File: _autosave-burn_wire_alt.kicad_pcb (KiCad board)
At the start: 2 copper layers, 24.5 x 24.5 mm, 16 parts, among them J1 TestPoint_THTPad_1.0x1.0mm_Dr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, J2 TestPoint_THTPad_1.0x1.0mm_Dr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, U1 ADP2303ARDZ

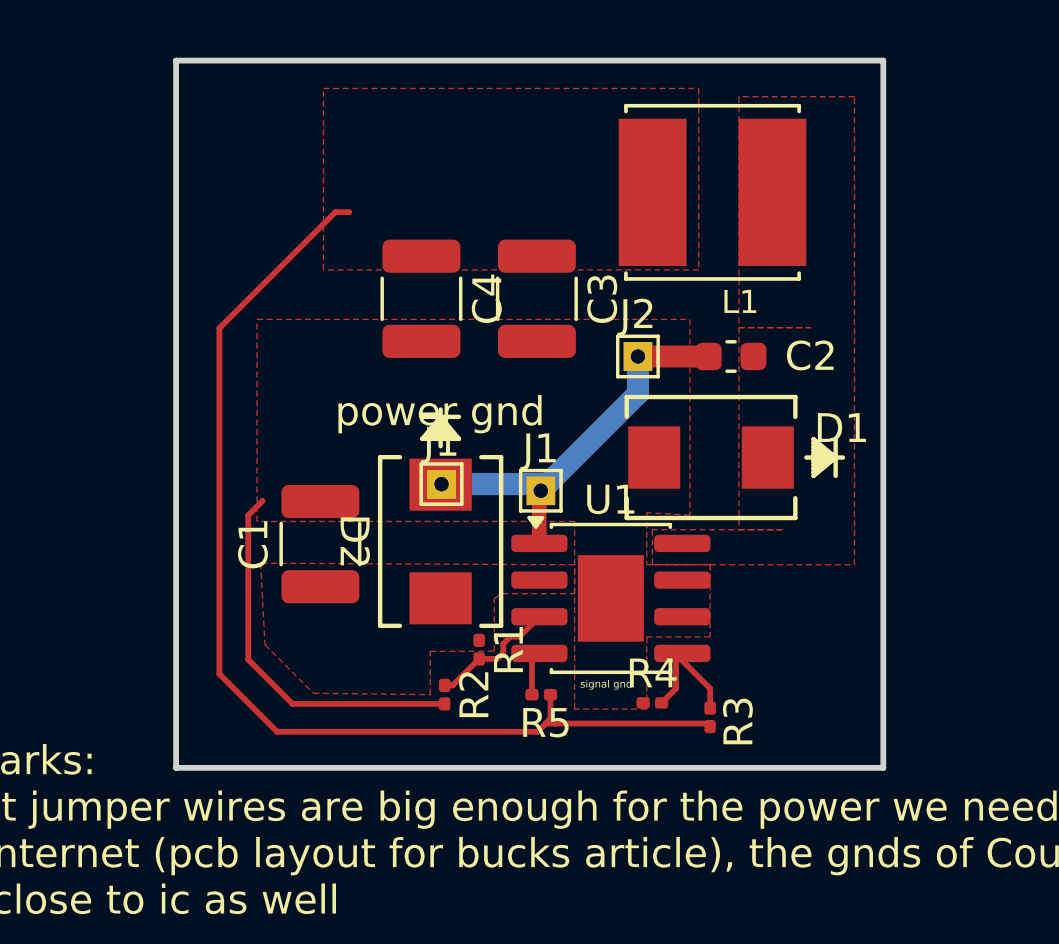
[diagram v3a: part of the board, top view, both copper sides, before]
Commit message: rounded corners
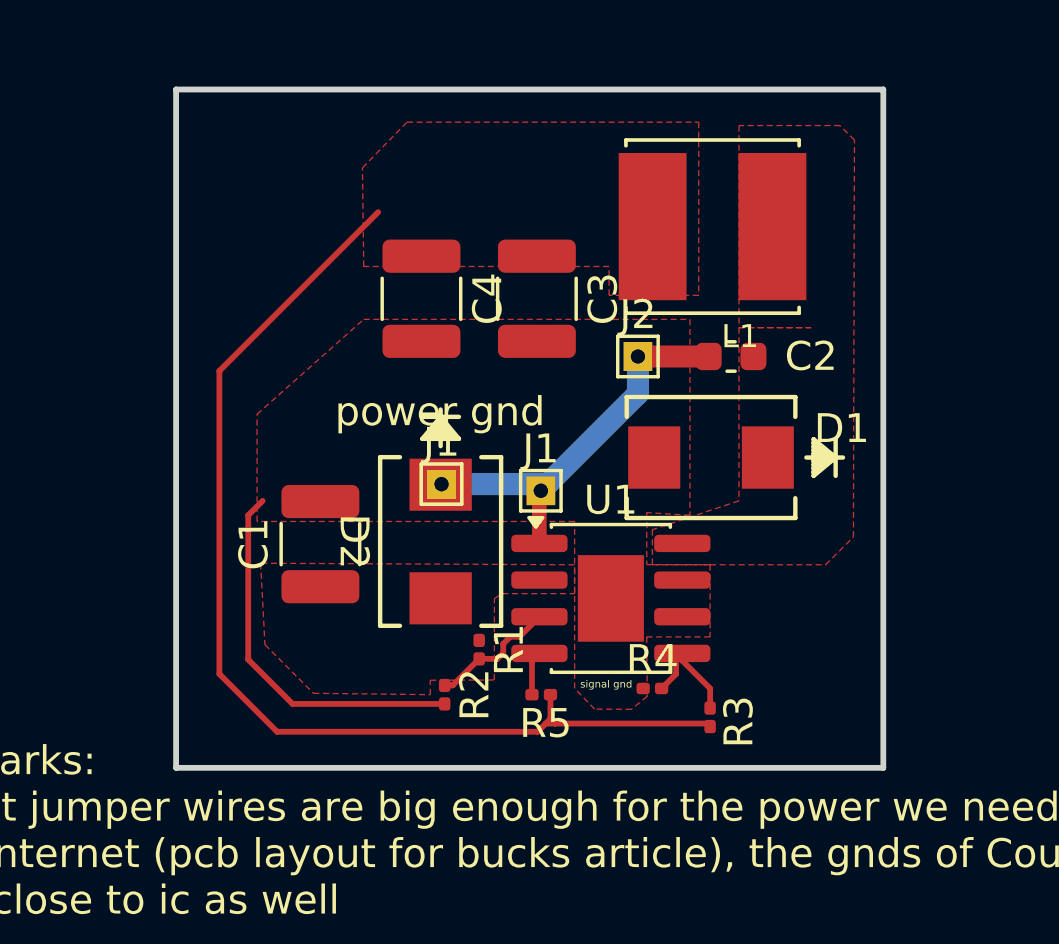
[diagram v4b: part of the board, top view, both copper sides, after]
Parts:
- moved L1 1.19 mm to (174.1, 81.5)
- moved R4 0.50 mm to (172.0, 97.5)
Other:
- board size 24.5 x 24.5 mm -> 24.5 x 23.5 mm
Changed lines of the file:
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@@
 			(layer "F.CrtYd")
 		)
-		(fp_text user "${REFERENCE}"
-			(at 0 -1.45 0)
+		(fp_text user "J3"
+			(at -0.696084 -0.422504 0)
 			(layer "F.Fab")
 			(effects
@@
 	(footprint "imported_footprints:IND_SRN6045TA-3R3Y"
 		(layer "F.Cu")
-		(at 174.083584 80.313715 180)
+		(at 174.083584 81.5 180)
 		(property "Reference" "L1"
 			(at -0.96 -3.808 0)
@@
 	(footprint "Resistor_SMD:R_0201_0603Metric"
 		(layer "F.Cu")
-		(at 172 98 180)
+		(at 172 97.5 180)
 		(descr "Resistor SMD 0201 (0603 Metric), square (rectangular) end terminal, IPC-7351 nominal, (Body size source: https://www.vishay.com/docs/20052/crcw0201e3.pdf)")
 		(tags "resistor")
@@
 	)
 	(gr_rect
-		(start 155.5 75.75)
+		(start 155.5 76.75)
 		(end 179.999999 100.25)
 		(stroke
@@
 	)
 	(segment
-		(start 168.47013 98.54987)
-		(end 168.63513 98.71487)
-		(width 0.2)
-		(layer "F.Cu")
-		(net "/Vout")
-	)
-	(segment
-		(start 161.02 81)
-		(end 157 85.02)
-		(width 0.2)
-		(layer "F.Cu")
-		(net "/Vout")
-	)
-	(segment
-		(start 168.47013 97.71487)
-		(end 168.47013 98.54987)
-		(width 0.2)
-		(layer "F.Cu")
-		(net "/Vout")
-	)
-	(segment
-		(start 168.02 99)
-		(end 168.30513 98.71487)
-		(width 0.2)
-		(layer "F.Cu")
-		(net "/Vout")
-	)
-	(segment
-		(start 159 99)
-		(end 168.02 99)
-		(width 0.2)
-		(layer "F.Cu")
-		(net "/Vout")
-	)
-	(segment
-		(start 173.89487 98.71487)
-		(end 168.63513 98.71487)
-		(width 0.2)
-		(layer "F.Cu")
-		(net "/Vout")
-	)
-	(segment
-		(start 157 85.02)
-		(end 157 97)
-		(width 0.2)
-		(layer "F.Cu")
-		(net "/Vout")
-	)
-	(segment
-		(start 168.30513 98.71487)
-		(end 168.63513 98.71487)
-		(width 0.2)
-		(layer "F.Cu")
-		(net "/Vout")
-	)
-	(segment
-		(start 161.5 81)
-		(end 161.02 81)
-		(width 0.2)
-		(layer "F.Cu")
-		(net "/Vout")
-	)
-	(segment
-		(start 174 98.82)
-		(end 173.89487 98.71487)
-		(width 0.2)
-		(layer "F.Cu")
-		(net "/Vout")
-	)
-	(segment
-		(start 168.47013 98.54987)
-		(end 168.30513 98.71487)
-		(width 0.2)
-		(layer "F.Cu")
-		(net "/Vout")
-	)
-	(segment
-		(start 157 97)
-		(end 159 99)
-		(width 0.2)
-		(layer "F.Cu")
-		(net "/Vout")
-	)
-	(segment
-		(start 158 96.5)
-		(end 158 91.5)
-		(width 0.2)
-		(layer "F.Cu")
-		(net "GND")
-	)
-	(segment
-		(start 158 91.5)
-		(end 158.5 91)
-		(width 0.2)
-		(layer "F.Cu")
-		(net "GND")
-	)
-	(segment
-		(start 164.80513 98.03487)
-		(end 159.53487 98.03487)
-		(width 0.2)
-		(layer "F.Cu")
-		(net "GND")
-	)
-	(segment
-		(start 159.53487 98.03487)
-		(end 158 96.5)
-		(width 0.2)
-		(layer "F.Cu")
-		(net "GND")
-	)
-	(segment
 		(start 168.136714 90.651297)
 		(end 168.081839 90.706172)
@@
 	)
 	(segment
+		(start 162.5 81)
+		(end 157 86.5)
+		(width 0.2)
+		(layer "F.Cu")
+		(net "/Vout")
+	)
+	(segment
+		(start 168.47013 98.54987)
+		(end 168.63513 98.71487)
+		(width 0.2)
+		(layer "F.Cu")
+		(net "/Vout")
+	)
+	(segment
+		(start 157 97)
+		(end 159 99)
+		(width 0.2)
+		(layer "F.Cu")
+		(net "/Vout")
+	)
+	(segment
+		(start 168.47013 97.71487)
+		(end 168.47013 98.54987)
+		(width 0.2)
+		(layer "F.Cu")
+		(net "/Vout")
+	)
+	(segment
+		(start 157 86.5)
+		(end 157 97)
+		(width 0.2)
+		(layer "F.Cu")
+		(net "/Vout")
+	)
+	(segment
+		(start 168.02 99)
+		(end 168.30513 98.71487)
+		(width 0.2)
+		(layer "F.Cu")
+		(net "/Vout")
+	)
+	(segment
+		(start 173.89487 98.71487)
+		(end 168.63513 98.71487)
+		(width 0.2)
+		(layer "F.Cu")
+		(net "/Vout")
+	)
+	(segment
+		(start 168.30513 98.71487)
+		(end 168.63513 98.71487)
+		(width 0.2)
+		(layer "F.Cu")
+		(net "/Vout")
+	)
+	(segment
+		(start 174 98.82)
+		(end 173.89487 98.71487)
+		(width 0.2)
+		(layer "F.Cu")
+		(net "/Vout")
+	)
+	(segment
+		(start 168.47013 98.54987)
+		(end 168.30513 98.71487)
+		(width 0.2)
+		(layer "F.Cu")
+		(net "/Vout")
+	)
+	(segment
+		(start 159 99)
+		(end 168.02 99)
+		(width 0.2)
+		(layer "F.Cu")
+		(net "/Vout")
+	)
+	(segment
+		(start 158 96.5)
+		(end 158 91.5)
+		(width 0.2)
+		(layer "F.Cu")
+		(net "GND")
+	)
+	(segment
+		(start 158 91.5)
+		(end 158.5 91)
+		(width 0.2)
+		(layer "F.Cu")
+		(net "GND")
+	)
+	(segment
+		(start 164.80513 98.03487)
+		(end 159.53487 98.03487)
+		(width 0.2)
+		(layer "F.Cu")
+		(net "GND")
+	)
+	(segment
+		(start 159.53487 98.03487)
+		(end 158 96.5)
+		(width 0.2)
+		(layer "F.Cu")
+		(net "GND")
+	)
+	(segment
 		(start 166.833811 96.26841)
 		(end 166.627221 96.475)
@@
 	)
 	(segment
-		(start 172.82 97.5)
-		(end 172.82 96.502221)
-		(width 0.2)
-		(layer "F.Cu")
-		(net "/FB")
-	)
-	(segment
 		(start 173.036611 96.536611)
 		(end 174 97.5)
@@
 	)
 	(segment
-		(start 172.32 98)
-		(end 172.82 97.5)
+		(start 172.82 96.502221)
+		(end 173.036611 96.28561)
+		(width 0.2)
+		(layer "F.Cu")
+		(net "/FB")
+	)
+	(segment
+		(start 172.32 97.5)
+		(end 172.82 97)
+		(width 0.2)
+		(layer "F.Cu")
+		(net "/FB")
+	)
+	(segment
+		(start 172.82 97)
+		(end 172.82 96.502221)
 		(width 0.2)
 		(layer "F.Cu")
@@
 		(start 174 97.5)
 		(end 174 98.18)
-		(width 0.2)
-		(layer "F.Cu")
-		(net "/FB")
-	)
-	(segment
-		(start 172.82 96.502221)
-		(end 173.036611 96.28561)
 		(width 0.2)
 		(layer "F.Cu")
@@
 		(polygon
 			(pts
-				(xy 158.30513 84.71487) (xy 170.30513 84.71487) (xy 170.305137 84.71487) (xy 173.303604 84.71487)
+				(xy 158.30513 88) (xy 162 84.71487) (xy 170.30513 84.71487) (xy 170.305137 84.71487) (xy 173.303604 84.71487)
 				(xy 173.304518 91.5) (xy 171.80513 91.409245) (xy 171.80513 93.208563) (xy 174 93.212518) (xy 174 95.71487)
-				(xy 171.80513 95.71487) (xy 171.80513 98.21487) (xy 169.30513 98.21487) (xy 169.30513 91.71487)
-				(xy 158.30513 91.71487)
+				(xy 171.80513 95.71487) (xy 171.821184 97.772697) (xy 171.273974 98.222932) (xy 170 98.21487) (xy 169.30513 97.5)
+				(xy 169.30513 91.71487) (xy 158.30513 91.71487)
 			)
 		)
@@
 		(polygon
 			(pts
-				(xy 173.60523 76.71487) (xy 173.60523 83) (xy 160.60523 83) (xy 160.60523 76.71487)
+				(xy 163.5 77.881501) (xy 173.60523 77.881501) (xy 173.60523 83.881501) (xy 170.5 83.881501) (xy 170.5 82.881501)
+				(xy 162 82.881501) (xy 161.956651 79.464511)
 			)
 		)
@@
 			(pts
 				(xy 169.30513 93.21487) (xy 158.429005 93.161993) (xy 158.578707 95.98336) (xy 160.258882 97.667374)
-				(xy 164.30513 97.71487) (xy 164.30513 96.214873) (xy 166.524562 96.207723) (xy 166.524562 94.385344)
+				(xy 164.30513 97.71487) (xy 164.30513 97.214876) (xy 166.524562 97.207726) (xy 166.524562 94.385344)
 				(xy 166.80513 94.21487) (xy 169.30513 94.21487)
 			)
@@
 		(polygon
 			(pts
-				(xy 172 92) (xy 172 93.21487) (xy 179 93.21487) (xy 179 77) (xy 175 77) (xy 175 85) (xy 177.5 85)
-				(xy 175 85) (xy 175 92) (xy 176.5 92)
-			)
-		)
+				(xy 172 92) (xy 172 93.21487) (xy 178 93.21487) (xy 178.964196 92.255505) (xy 179 78.5) (xy 178.5 78)
+				(xy 175 78) (xy 175 85) (xy 177.5 85) (xy 175 85) (xy 175 91)
+			)
+		)

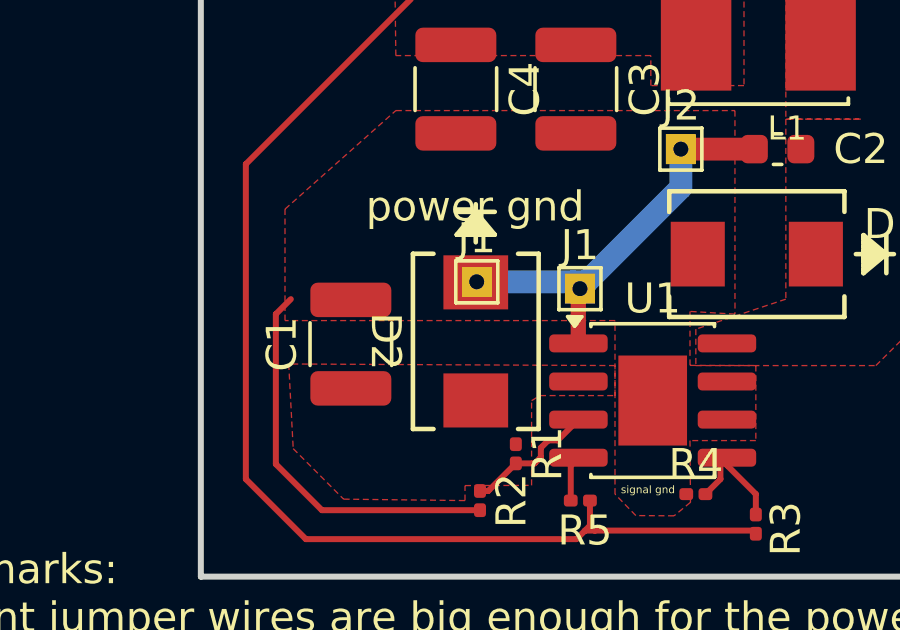
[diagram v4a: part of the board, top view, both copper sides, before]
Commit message: added bst plane under bst diode
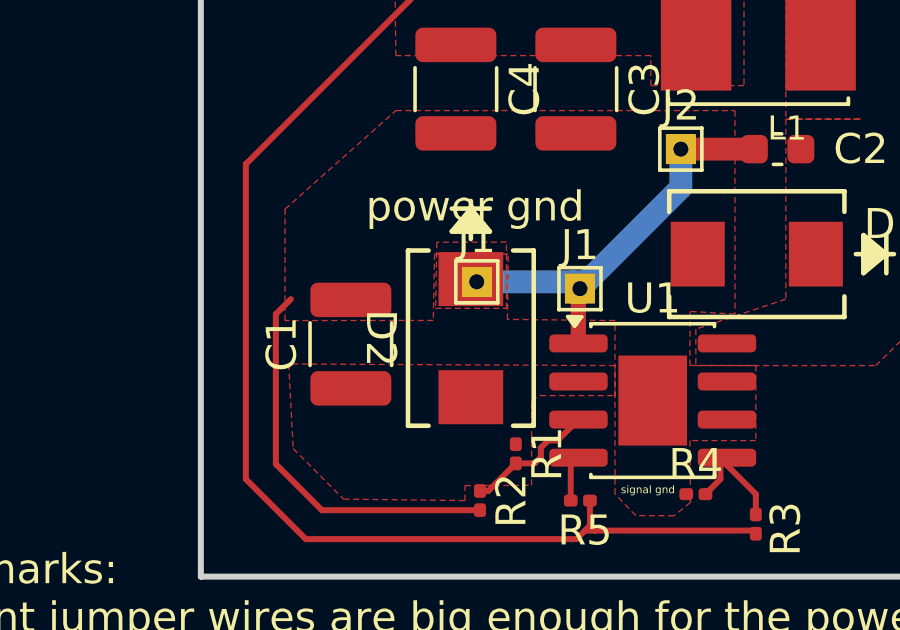
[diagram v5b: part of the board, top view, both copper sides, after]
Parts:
- moved D2 0.20 mm to (164.5, 92.3)
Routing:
- added copper zone on F.Cu, net /BST
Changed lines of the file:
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@@
 	(footprint "imported_footprints:CR_SMB_320-345BE_DIO-L"
 		(layer "F.Cu")
-		(at 164.664534 92.408744 -90)
+		(at 164.5 92.3001 -90)
 		(tags "B330B-13-F ")
 		(property "Reference" "D2"
@@
 				(xy 173.304518 91.5) (xy 171.80513 91.409245) (xy 171.80513 93.208563) (xy 174 93.212518) (xy 174 95.71487)
 				(xy 171.80513 95.71487) (xy 171.821184 97.772697) (xy 171.273974 98.222932) (xy 170 98.21487) (xy 169.30513 97.5)
-				(xy 169.30513 91.71487) (xy 158.30513 91.71487)
-			)
-		)
+				(xy 169.30513 91.71487) (xy 165.72021 91.67415) (xy 165.744922 89.498664) (xy 163.29022 89.500218)
+				(xy 163.249204 91.710216) (xy 158.30513 91.71487)
+			)
+		)
+	)
+	(zone
+		(net "/BST")
+		(layer "F.Cu")
+		(hatch edge 0.5)
+		(connect_pads yes
+			(clearance 0.254)
+		)
+		(min_thickness 0.25)
+		(fill yes
+			(thermal_gap 0.5)
+			(thermal_bridge_width 0.5)
+			(island_removal_mode 0)
+		)
+		(polygon
+			(pts
+				(xy 163.366117 89.103415) (xy 163.325102 91.306783) (xy 165.687756 91.306783) (xy 165.687756 89.098543)
+			)
+		)

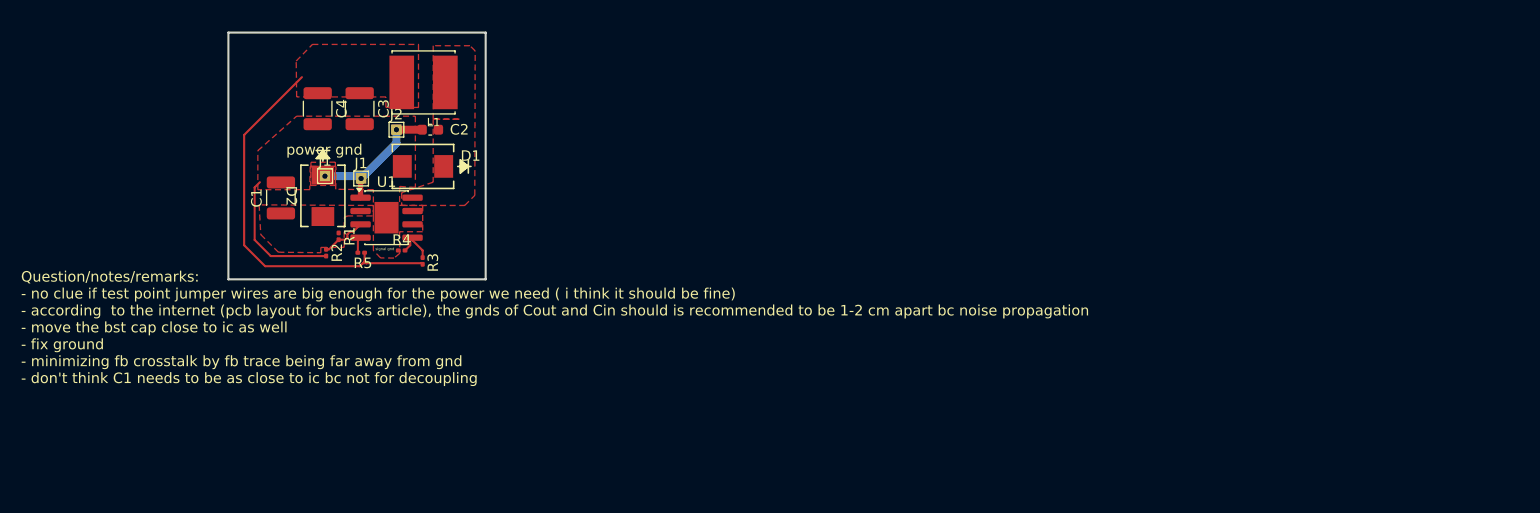
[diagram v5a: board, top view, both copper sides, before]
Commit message: cout connected to agnd
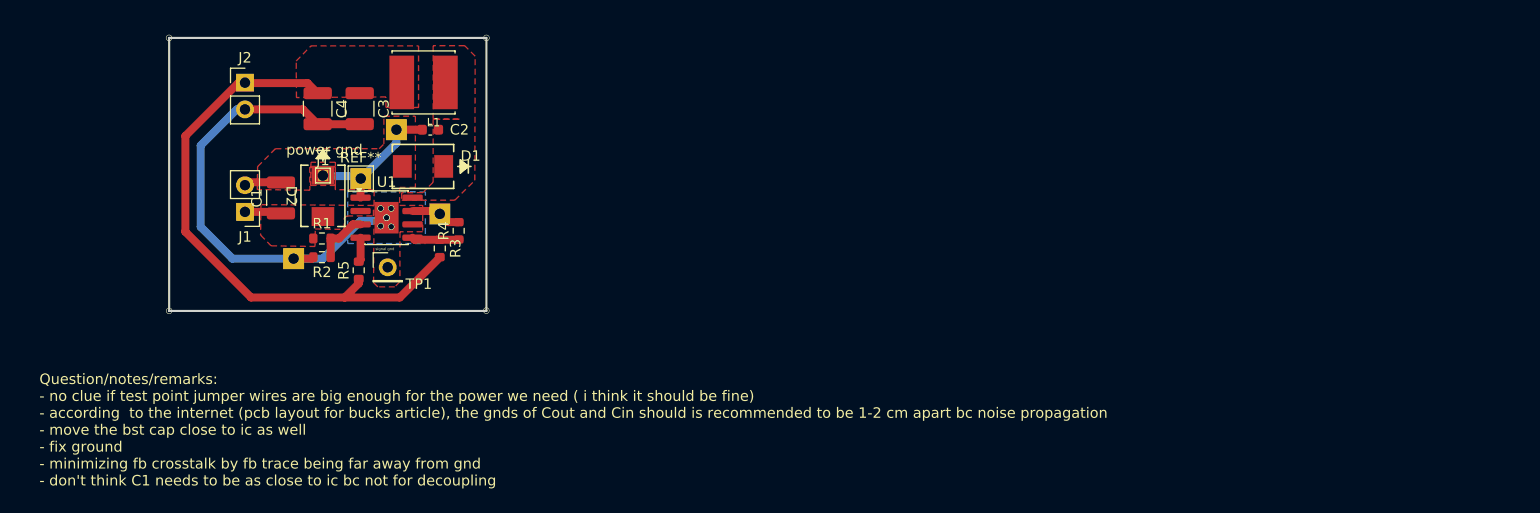
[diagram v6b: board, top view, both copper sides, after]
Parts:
- added ?: , , F.Cu at (171.5, 86.0)
- added ?: , , F.Cu at (175.6, 94.0)
- added ?: , , F.Cu at (161.7, 98.3)
- added REF**: TestPoint_THTPad_2.0x2.0mm_Drill1.0mm, TestPoint:TestPoint_THTPad_2.0x2.0mm_Drill1.0mm, F.Cu at (168.1, 90.7)
- added TP1: PinHeader_1x01_P2.54mm_Vertical, Connector_PinHeader_2.54mm:PinHeader_1x01_P2.54mm_Vertical, F.Cu at (170.7, 99.1)
- J1, J2: value TestPoint_THTPad_1.0x1.0mm_Drill0.5mm -> Conn_01x02_Pin; footprint TestPoint:TestPoint_THTPad_1.0x1.0mm_Drill0.5mm -> Connector_PinHeader_2.54mm:PinHeader_1x02_P2.54mm_Vertical
- R1, R2, R3, R4, R5: footprint Resistor_SMD:R_0201_0603Metric -> Resistor_SMD:R_0603_1608Metric
- moved J2 15.1 mm to (157.1, 81.5)
- moved J1 11.5 mm to (157.1, 93.8), turned to 180 degrees
- moved R4 5.74 mm to (177.4, 95.6), turned to 90 degrees
- moved R3 2.02 mm to (175.6, 97.3)
- moved R5 1.69 mm to (167.9, 99.4), turned to 90 degrees
- moved R1 1.60 mm to (164.4, 96.4), turned to 0 degrees
- moved R2 0.58 mm to (164.4, 98.1), turned to 180 degrees
- moved J1 0.21 mm to (164.5, 90.4)
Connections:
- J1 pad 1: /BST -> /Vin
- J2 pad 1: /BST -> /Vout
- U1 pad 6: GND -> unconnected-(U1-NC-Pad6)
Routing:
- net GND: track 13.1 -> 55.8 mm, vias 0 -> 9
- net /Vout: track 37.6 -> 55.0 mm
- net /Vin: track 0.00 -> 3.48 mm
- net /PGOOD: track 1.54 -> 2.35 mm
- net /FB: track 3.80 -> 4.49 mm
- net /EN: track 4.51 -> 5.19 mm
- added copper zone on B.Cu, net GND
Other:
- board size 24.5 x 23.5 mm -> 30.2 x 26 mm
